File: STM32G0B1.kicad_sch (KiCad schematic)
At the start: 23 parts, among them J1 Conn_ST_STDC14, J2 USB4105-GF-A, SW1 TS-1088-AR02016, U1 STM32H563RITx, U2 SRV05-4-P-T7, Y1 32.768kHz

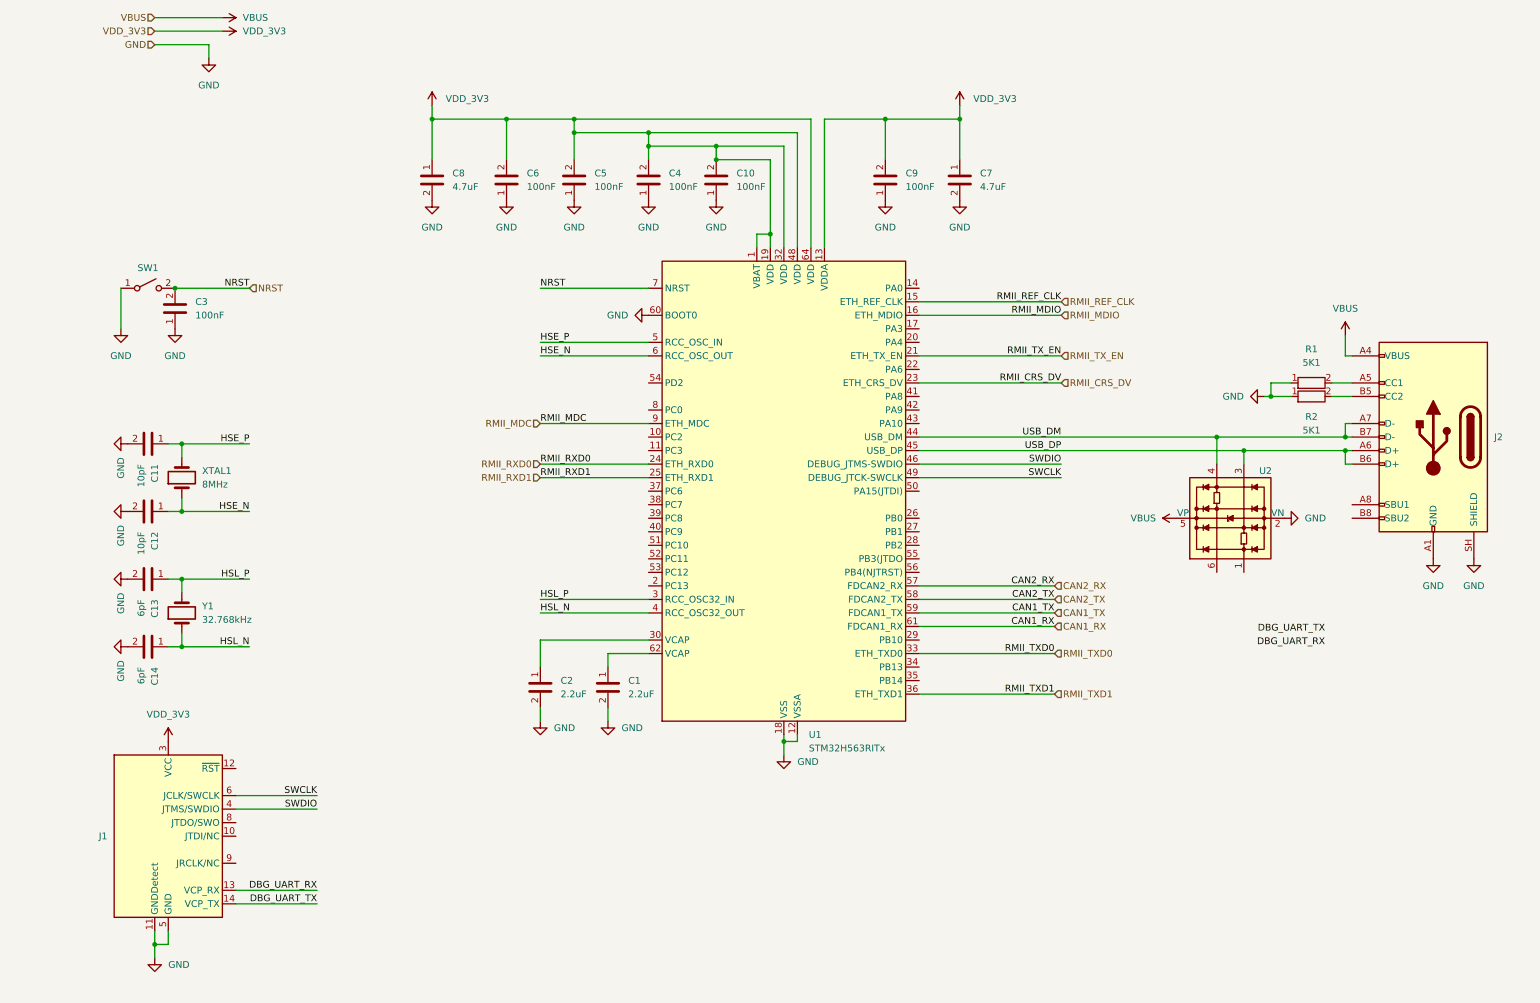
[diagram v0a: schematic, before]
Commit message: feat: added MVP routing implementation
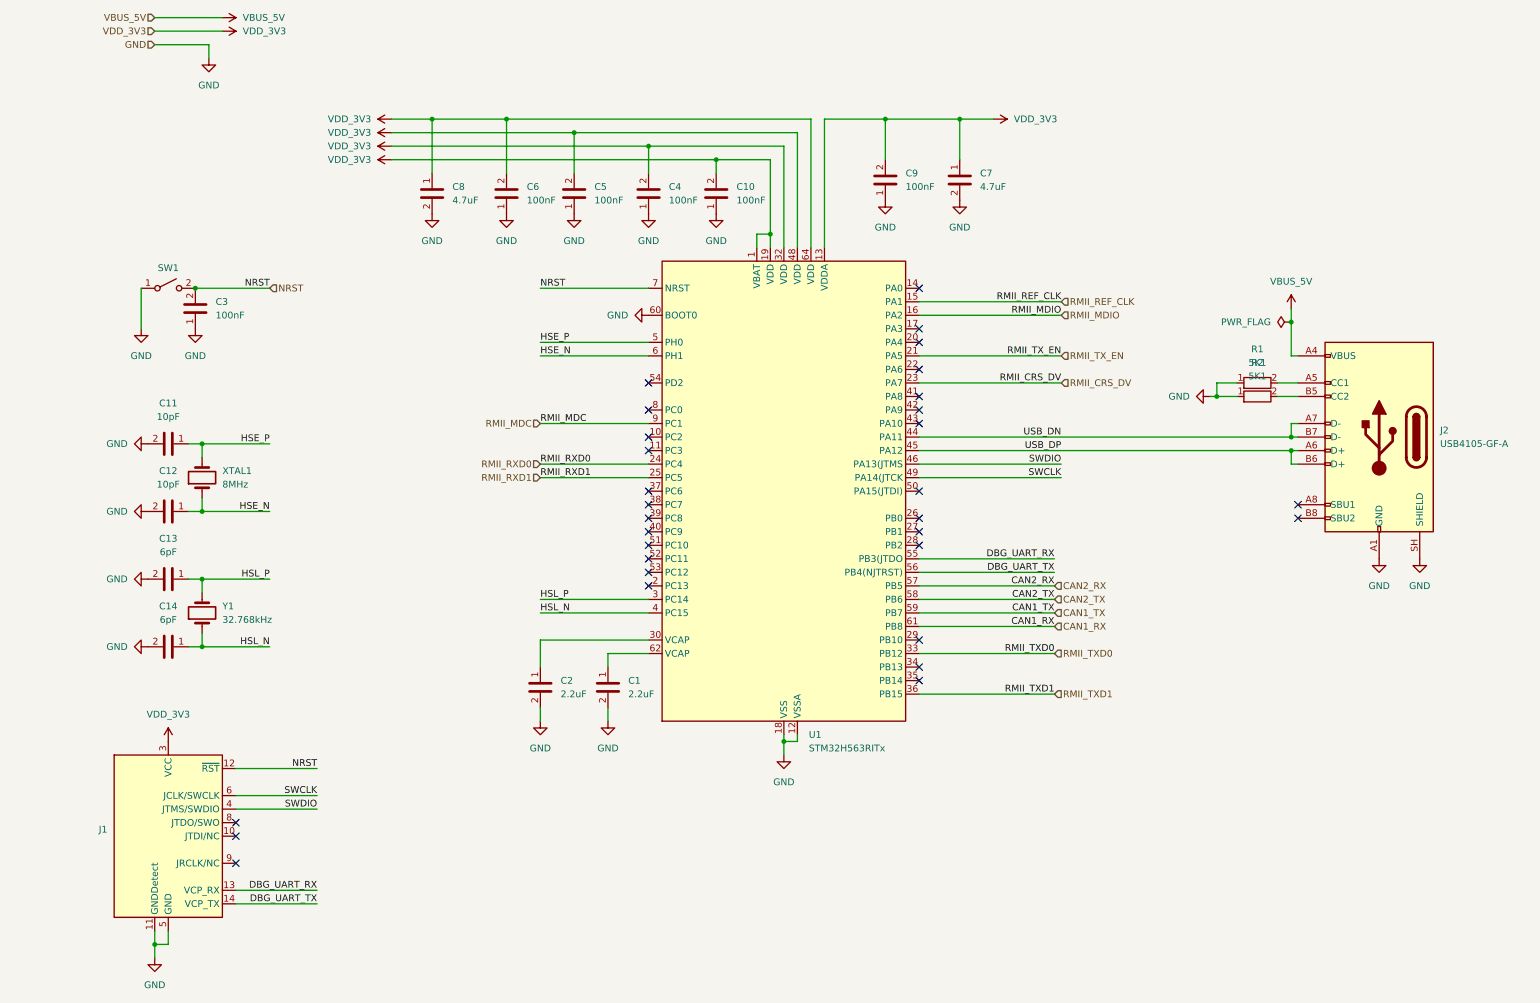
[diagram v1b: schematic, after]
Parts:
- removed U2: SRV05-4-P-T7, Package_TO_SOT_SMD:SC-74-6_1.55x2.9mm_P0.95mm, symbol 0_chenry_lib:SRV05-4-P-T7
- U1: symbol MCU_ST_STM32H5:STM32H563RITx -> 0_chenry_lib:STM32H563RITx; JLC_PN (none) -> C20619634
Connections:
- net DBG_UART_RX: now also U1.55 (PB3(JTDO)
- net DBG_UART_TX: now also U1.56 (PB4(NJTRST))
- net NRST: now also J1.12 (~{RST})
- net USB_DM renamed USB_DN
- net VBUS renamed VBUS_5V
- no-connect marks 0 -> 31
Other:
- moved on the sheet: C10, C11, C12, C13, C14, C3, C4, C5, C6, C8, J2, R1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

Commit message: fix: final polishes for MFR
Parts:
- added D4, D5, D6: LED_RED_0603, LED_SMD:LED_0603_1608Metric, symbol 0_chenry_lib:LED_RED_0603
- added R20, R21, R22: 5K1, chenry-footprint-lib:R_0402, symbol 0_chenry_lib:R_0402_5K1
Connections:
- net GND: now also R20.2, R21.2, R22.2
- net LED_0: now reaches U1.34 (PB13)
- net LED_0: now also D4.2 (A)
- net LED_1: now reaches U1.35 (PB14)
- net LED_1: now also D5.2 (A)
- net LED_2: now reaches U1.37 (PC6)
- net LED_2: now also D6.2 (A)
- new net: D5.1 (K), R21.1
- new net: D4.1 (K), R20.1
- new net: D6.1 (K), R22.1
- no-connect marks 31 -> 28

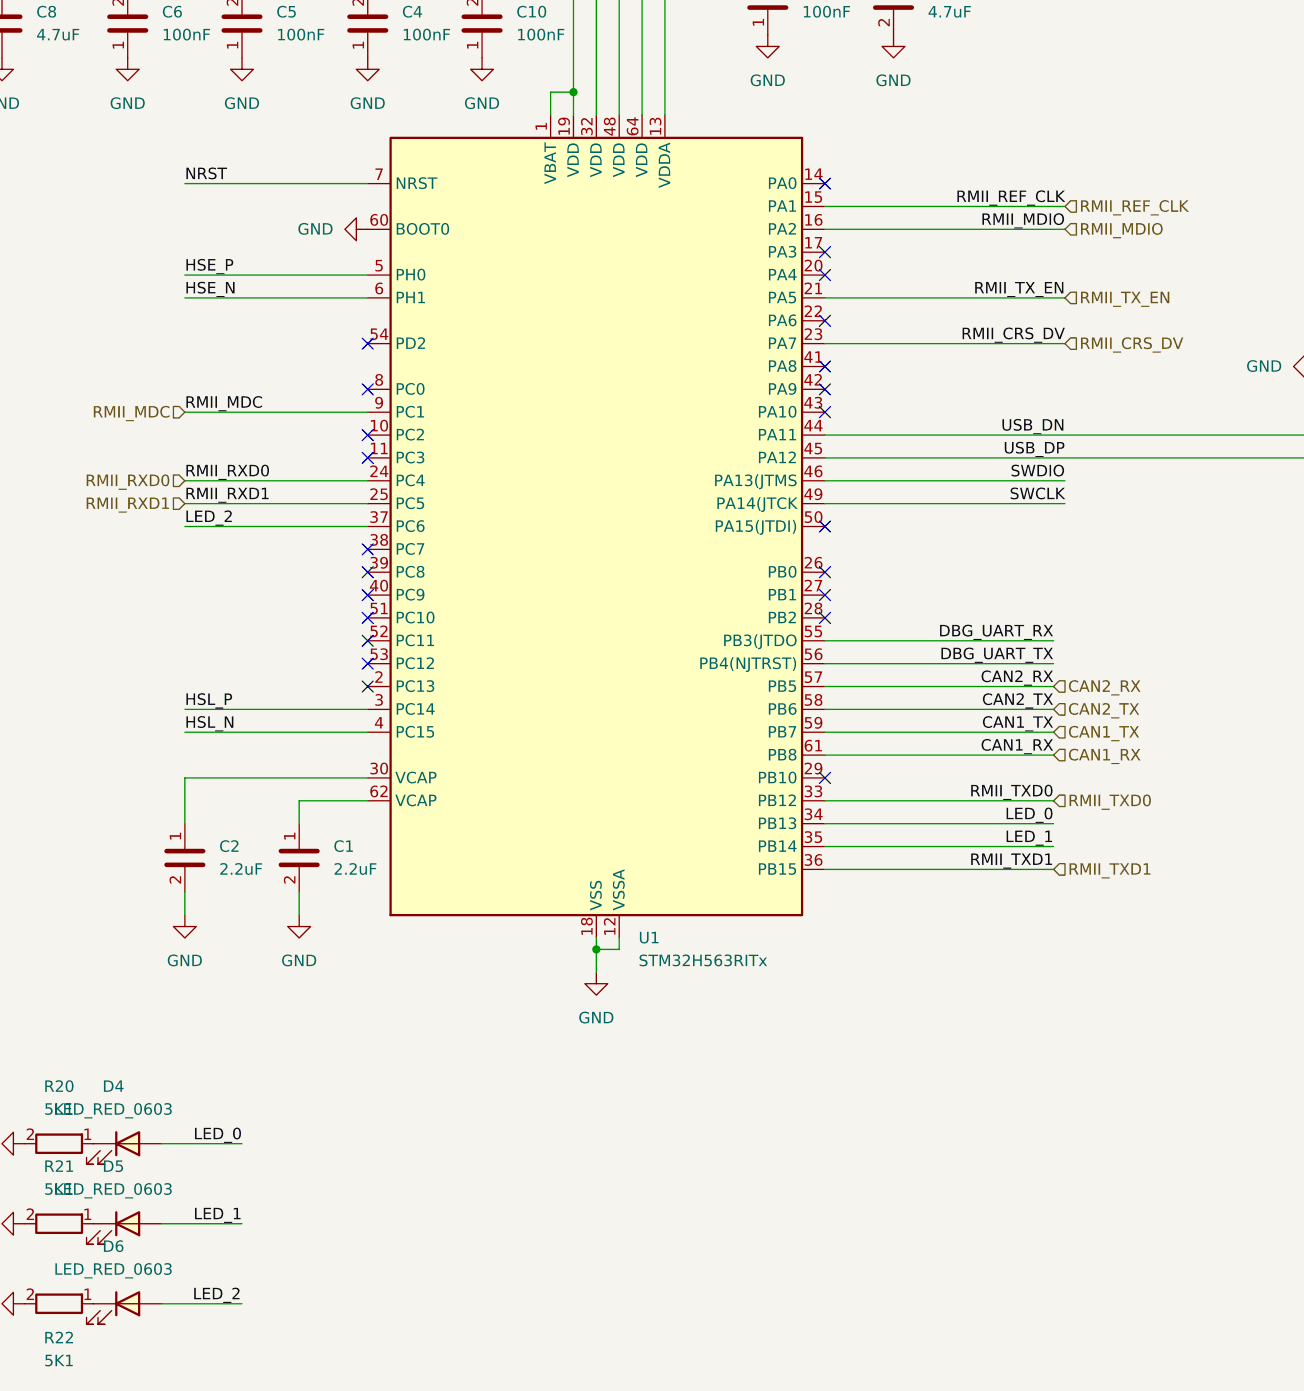
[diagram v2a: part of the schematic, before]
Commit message: fix: updated 12pin connector footprint + fix drc and exposed vias
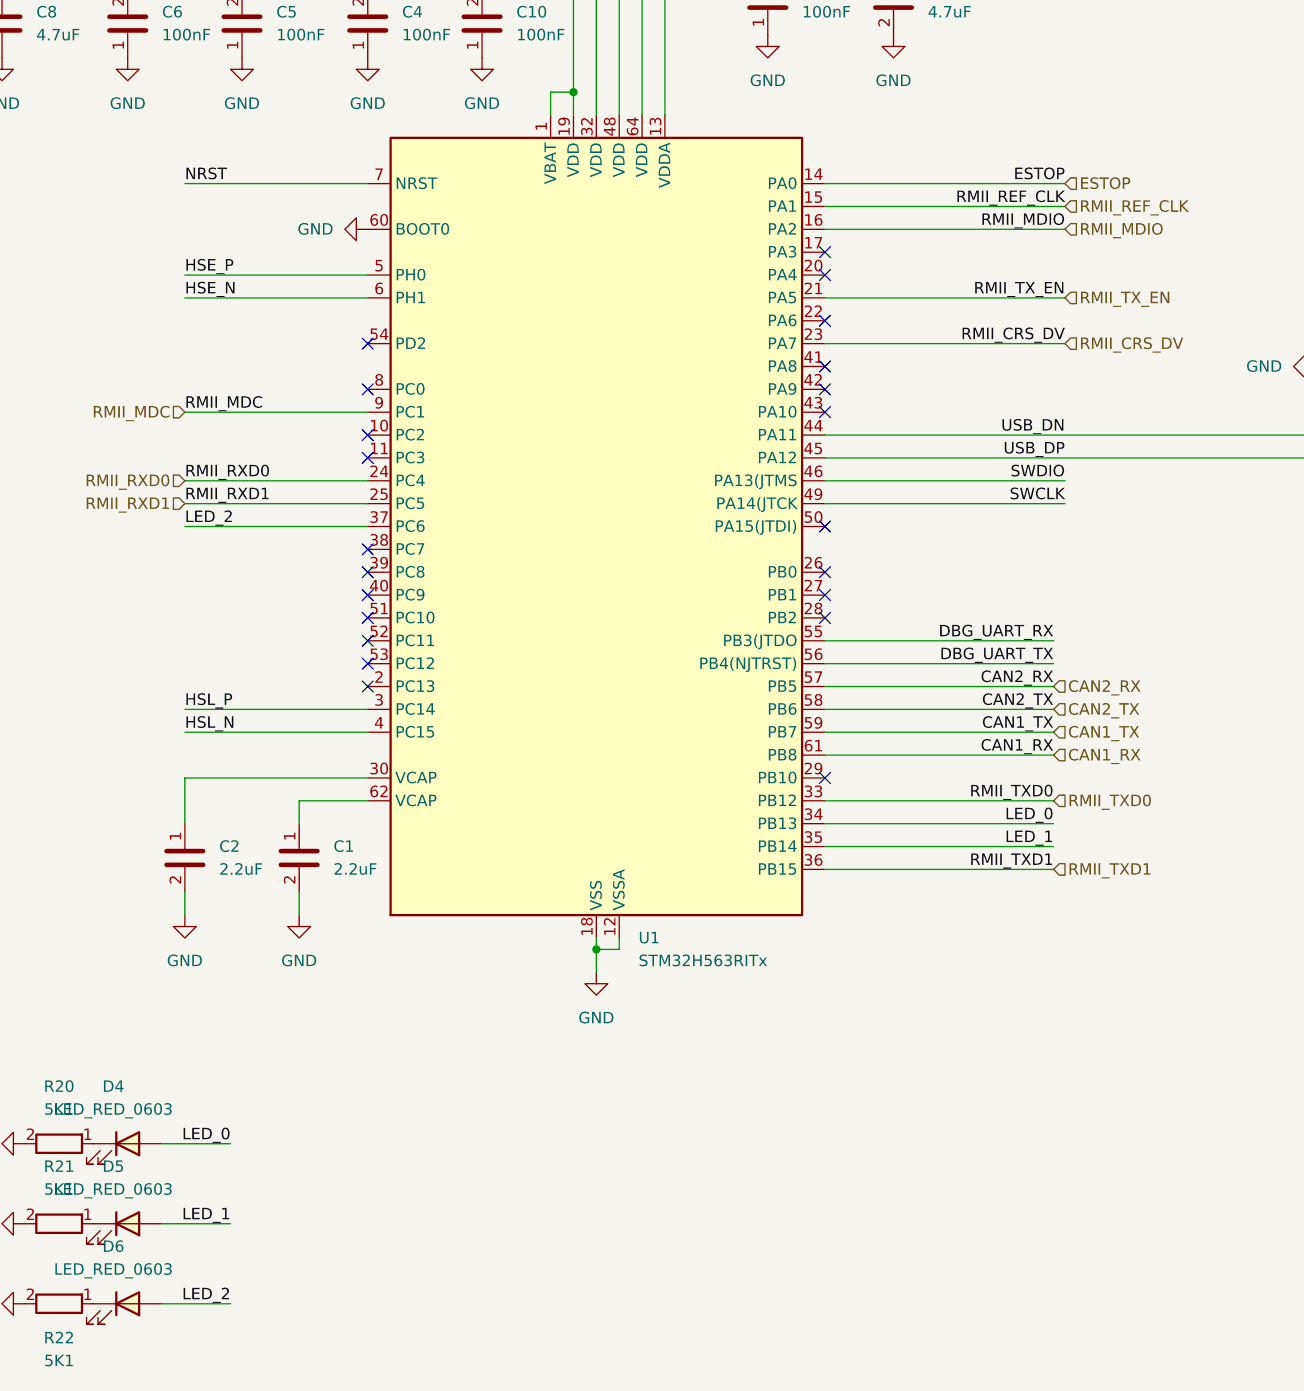
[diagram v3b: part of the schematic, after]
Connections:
- net ESTOP: now reaches U1.14 (PA0)
- no-connect marks 28 -> 27
